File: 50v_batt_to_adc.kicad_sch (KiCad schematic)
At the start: 10 parts

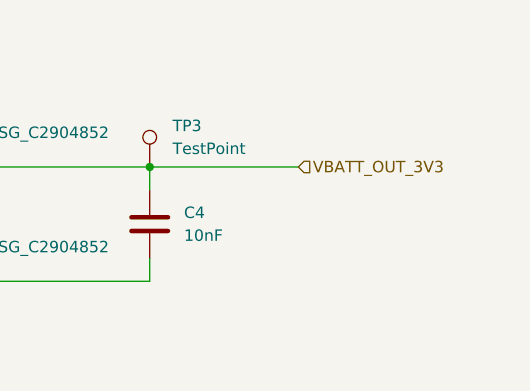
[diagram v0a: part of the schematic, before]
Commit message: Place opto couplers and some connectors.
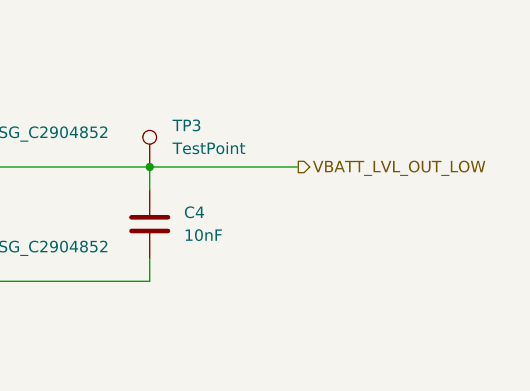
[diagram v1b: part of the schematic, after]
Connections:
- net VBATT_OUT_3V3 renamed VBATT_LVL_OUT_LOW
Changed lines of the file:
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@@
 		)
 	)
-	(hierarchical_label "VBATT_OUT_3V3"
-		(shape input)
+	(hierarchical_label "VBATT_LVL_OUT_LOW"
+		(shape output)
 		(at 189.23 80.01 0)
 		(effects

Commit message: Push schematic stuff missed before.
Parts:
- added C10: 100nF, Capacitor_SMD:C_0805_2012Metric, symbol Device:C
- FB1: value FerriteBead_Small -> BLM18PG121SN1D; LCSC (none) -> C14709
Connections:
- net GND: now also C10.2
- net VBATT_LVL_OUT_LOW: now also C10.1
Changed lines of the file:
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@@
+	)
+	(junction
+		(at 172.72 92.71)
+		(diameter 0)
+		(color 0 0 0 0)
+	)
+	(junction
+		(at 184.15 80.01)
+		(diameter 0)
+		(color 0 0 0 0)
 	)
 	(junction
@@
 	(wire
 		(pts
+			(xy 184.15 90.17) (xy 184.15 92.71)
+		)
+		(stroke
+			(width 0)
+			(type default)
+		)
+	)
+	(wire
+		(pts
 			(xy 144.78 80.01) (xy 144.78 82.55)
 		)
@@
 	(wire
 		(pts
+			(xy 184.15 80.01) (xy 189.23 80.01)
+		)
+		(stroke
+			(width 0)
+			(type default)
+		)
+	)
+	(wire
+		(pts
 			(xy 59.69 80.01) (xy 67.31 80.01)
 		)
@@
 	(wire
 		(pts
-			(xy 172.72 80.01) (xy 189.23 80.01)
+			(xy 172.72 80.01) (xy 184.15 80.01)
+		)
+		(stroke
+			(width 0)
+			(type default)
+		)
+	)
+	(wire
+		(pts
+			(xy 172.72 92.71) (xy 184.15 92.71)
 		)
 		(stroke
@@
 		(pts
 			(xy 110.49 80.01) (xy 114.3 80.01)
+		)
+		(stroke
+			(width 0)
+			(type default)
+		)
+	)
+	(wire
+		(pts
+			(xy 184.15 80.01) (xy 184.15 82.55)
 		)
 		(stroke
@@
 	)
 	(symbol
+		(lib_id "Device:C")
+		(at 184.15 86.36 0)
+		(unit 1)
+		(exclude_from_sim no)
+		(in_bom yes)
+		(on_board yes)
+		(dnp no)
+		(fields_autoplaced yes)
+		(property "Reference" "C10"
+			(at 187.96 85.0899 0)
+			(effects
+				(font
+					(size 1.27 1.27)
+				)
+				(justify left)
+			)
+		)
+		(property "Value" "100nF"
+			(at 187.96 87.6299 0)
+			(effects
+				(font
+					(size 1.27 1.27)
+				)
+				(justify left)
+			)
+		)
+		(property "Footprint" "Capacitor_SMD:C_0805_2012Metric"
+			(at 185.1152 90.17 0)
+			(effects
+				(font
+					(size 1.27 1.27)
+				)
+				(hide yes)
+			)
+		)
+		(property "Datasheet" "https://jlcpcb.com/partdetail/YAGEO-CC0603KRX7R9BB104/C14663"
+			(at 184.15 86.36 0)
+			(effects
+				(font
+					(size 1.27 1.27)
+				)
+				(hide yes)
+			)
+		)
+		(property "Description" "Unpolarized capacitor"
+			(at 184.15 86.36 0)
+			(effects
+				(font
+					(size 1.27 1.27)
+				)
+				(hide yes)
+			)
+		)
+		(property "LCSC" "C14663"
+			(at 184.15 86.36 0)
+			(effects
+				(font
+					(size 1.27 1.27)
+				)
+				(hide yes)
+			)
+		)
+		(pin "1"
+		)
+		(pin "2"
+		)
+		(instances
+			(project "stopnu-hardware"
+				(path "/4ab90003-ea4c-4878-8117-f834ac24f8d9/b19922b5-b274-4778-931e-95ff57c7d649"
+					(reference "C10")
+					(unit 1)
+				)
+			)
+		)
+	)
+	(symbol
 		(lib_id "Connector:TestPoint")
 		(at 172.72 80.01 0)
@@
 			)
 		)
-		(property "Value" "FerriteBead_Small"
+		(property "Value" "BLM18PG121SN1D"
 			(at 87.6681 76.2 90)
 			(effects
@@
 			)
 		)
-		(property "Datasheet" "~"
+		(property "Datasheet" "https://jlcpcb.com/partdetail/MurataElectronics-BLM18PG121SN1D/C14709"
 			(at 87.63 80.01 0)
 			(effects
@@
 		(property "Description" "Ferrite bead, small symbol"
 			(at 87.63 80.01 0)
+			(effects
+				(font
+					(size 1.27 1.27)
+				)
+				(hide yes)
+			)
+		)
+		(property "LCSC" "C14709"
+			(at 87.63 80.01 90)
 			(effects
 				(font
@@
 			)
 		)
-		(property "Datasheet" ""
+		(property "Datasheet" "https://www.lcsc.com/product-detail/C2904852.html?s_z=n_C2904852"
 			(at 144.78 87.63 0)
 			(effects
@@
 			)
 		)
-		(property "Description" ""
+		(property "Description" "Shikues 1N4148WSG"
 			(at 144.78 87.63 0)
 			(effects
@@
 			)
 		)
-		(property "Datasheet" ""
+		(property "Datasheet" "https://www.lcsc.com/product-detail/C2904852.html?s_z=n_C2904852"
 			(at 144.78 74.93 0)
 			(effects
@@
 			)
 		)
-		(property "Description" ""
+		(property "Description" "Shikues 1N4148WSG"
 			(at 144.78 74.93 0)
 			(effects
